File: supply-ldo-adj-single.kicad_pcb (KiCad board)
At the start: 2 copper layers, 31.8 x 33 mm, 15 parts, among them P1 CONN_02X02, P2 CONN_01X03, P3 CONN_02X08, P4 CONN_02X04, P5 CONN_01X01, P6 CONN_01X01, U1 TPS7A4700

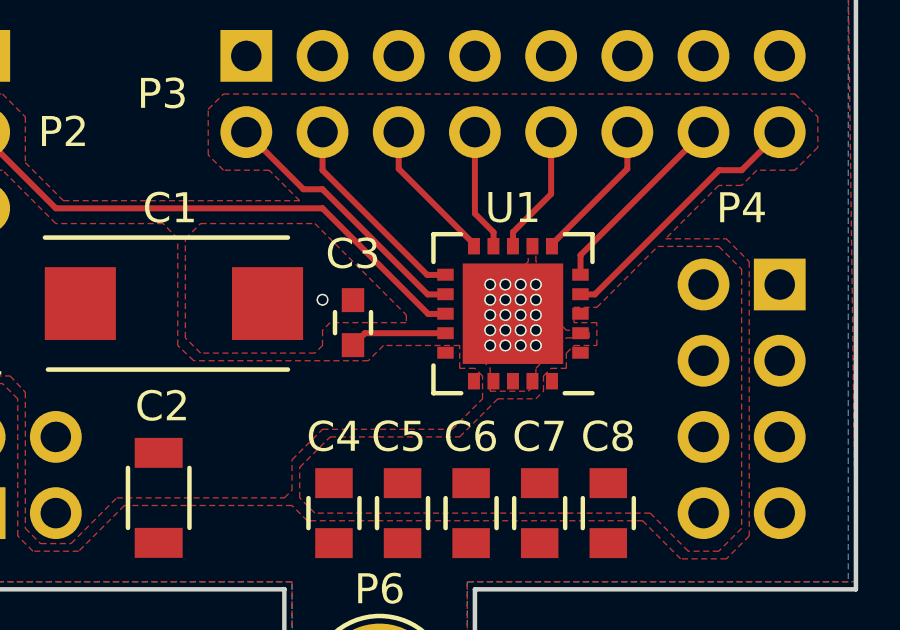
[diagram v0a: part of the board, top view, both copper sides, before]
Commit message: Reduce via size, verbose info on silkscreen
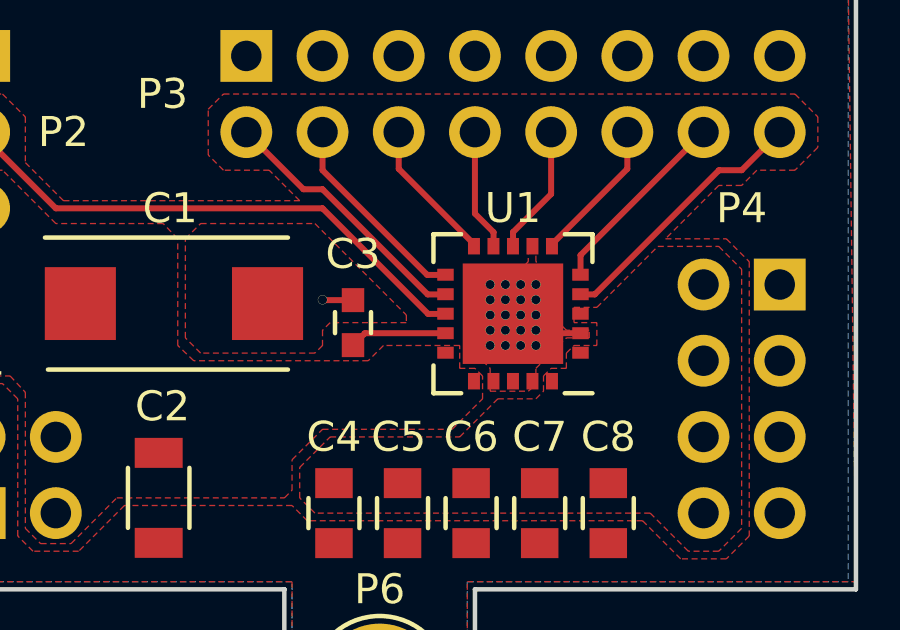
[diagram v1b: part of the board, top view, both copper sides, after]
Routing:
- net GND: track 0.00 -> 2.51 mm
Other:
- net class Thermal added: clearance 0.2, trace_width 0.2, via_dia 0.31, via_drill 0.3
- rule via_min_size: 0.4 -> 0.31
- board text added: "EN"
- board text added: "Low Dropout Adjustable Single Power Supply"
- board text added: "Vadj"
- board text added: "Vin≤36v"
- board text added: "Vout=Vadj+1.6"
- board text removed: "Vin"
- board text removed: "Vout"
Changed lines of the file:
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@@
-(kicad_pcb (version 4) (host pcbnew 4.0.2-stable)
+(kicad_pcb (version 4) (host pcbnew 4.0.1-stable)
   (general
     (links 58)
-    (no_connects 2)
+    (no_connects 0)
     (area 68.551667 20.244999 105.438334 53.934)
     (thickness 1.6)
-    (drawings 22)
-    (tracks 52)
+    (drawings 25)
+    (tracks 56)
     (zones 0)
     (modules 15)
@@
     (via_size 0.4)
     (via_drill 0.3)
-    (via_min_size 0.4)
+    (via_min_size 0.31)
     (via_min_drill 0.3)
     (uvia_size 0.508)
@@
     (pad_to_mask_clearance 0.2)
     (aux_axis_origin 0 0)
-    (visible_elements FFFFFF7F)
+    (visible_elements 7FFFFF5F)
     (pcbplotparams
       (layerselection 0x010fc_80000001)
@@
     (add_net "Net-(P6-Pad1)")
   )
+  (net_class Thermal ""
+    (clearance 0.2)
+    (trace_width 0.2)
+    (via_dia 0.31)
+    (via_drill 0.3)
+    (uvia_dia 0.508)
+    (uvia_drill 0.127)
+  )
   (module Capacitors_Tantalum_SMD:TantalC_SizeD_EIA-7343_Reflow (layer F.Cu)
     (at 80.137 37.465)
@@
       (net 5 "Net-(P6-Pad1)"))
   )
-  (gr_text "GPLv3\n©2016\nNESH@NJIT" (at 86.868 43.688) (layer B.SilkS)
-    (effects (font (size 1 1) (thickness 0.2)) (justify mirror))
-  )
-  (gr_text On (at 76.454 33.02) (layer B.SilkS)
-    (effects (font (size 1 1) (thickness 0.2)) (justify mirror))
-  )
-  (gr_text Off (at 76.708 30.48) (layer B.SilkS)
-    (effects (font (size 1 1) (thickness 0.2)) (justify mirror))
+  (gr_text EN (at 76.2 31.75) (layer B.SilkS)
+    (effects (font (size 0.8 0.8) (thickness 0.2)) (justify mirror))
+  )
+  (gr_text "GPLv3\n©2016\nNESH@NJIT" (at 87.122 44.831) (layer B.SilkS)
+    (effects (font (size 0.8 0.8) (thickness 0.2)) (justify mirror))
+  )
+  (gr_text Vadj (at 91.44 35.433) (layer B.SilkS)
+    (effects (font (size 0.8 0.8) (thickness 0.2)) (justify mirror))
+  )
+  (gr_text "Low Dropout Adjustable\nSingle Power Supply" (at 87.122 40.386) (layer B.SilkS)
+    (effects (font (size 0.8 0.8) (thickness 0.2)) (justify mirror))
+  )
+  (gr_text On (at 76.2 34.29) (layer B.SilkS)
+    (effects (font (size 0.8 0.8) (thickness 0.2)) (justify mirror))
+  )
+  (gr_text Off (at 76.454 29.21) (layer B.SilkS)
+    (effects (font (size 0.8 0.8) (thickness 0.2)) (justify mirror))
   )
   (gr_text ⏚ (at 73.66 46.355) (layer B.SilkS)
@@
     (effects (font (size 1 1) (thickness 0.2)) (justify mirror))
   )
-  (gr_text Vin (at 78.74 43.18) (layer B.SilkS)
-    (effects (font (size 1 1) (thickness 0.2)) (justify mirror))
+  (gr_text Vin≤36v (at 74.93 39.624) (layer B.SilkS)
+    (effects (font (size 0.8 0.8) (thickness 0.2)) (justify mirror))
   )
   (gr_text ⏚ (at 100.33 46.355) (layer B.SilkS)
@@
     (effects (font (size 1 1) (thickness 0.2)) (justify mirror))
   )
-  (gr_text Vout (at 94.488 40.64) (layer B.SilkS)
-    (effects (font (size 1 1) (thickness 0.2)) (justify mirror))
+  (gr_text Vout=Vadj+1.6 (at 95.504 40.64 270) (layer B.SilkS)
+    (effects (font (size 0.8 0.8) (thickness 0.2)) (justify mirror))
   )
   (gr_text "6.4 6.4 3.2 1.6 0.8 0.4 0.2 0.1" (at 91.44 34.036) (layer B.SilkS)
-    (effects (font (size 1 0.85) (thickness 0.2)) (justify mirror))
+    (effects (font (size 0.8 0.8) (thickness 0.2)) (justify mirror))
   )
   (gr_line (start 102.87 46.99) (end 102.87 26.67) (layer Edge.Cuts) (width 0.15))
@@
   (gr_line (start 90.17 26.67) (end 90.17 20.32) (layer Edge.Cuts) (width 0.15))
   (gr_line (start 102.87 26.67) (end 90.17 26.67) (layer Edge.Cuts) (width 0.15))
-  (via (at 85.09 37.338) (size 0.4) (drill 0.3) (layers F.Cu B.Cu) (net 1))
-  (via (at 92.202 38.862) (size 0.4) (drill 0.3) (layers F.Cu B.Cu) (net 1) (status 30))
-  (via (at 91.694 38.862) (size 0.4) (drill 0.3) (layers F.Cu B.Cu) (net 1) (status 30))
-  (via (at 91.186 38.862) (size 0.4) (drill 0.3) (layers F.Cu B.Cu) (net 1) (status 30))
-  (via (at 90.678 38.862) (size 0.4) (drill 0.3) (layers F.Cu B.Cu) (net 1) (status 30))
-  (via (at 92.202 36.83) (size 0.4) (drill 0.3) (layers F.Cu B.Cu) (net 1) (status 30))
-  (via (at 91.694 36.83) (size 0.4) (drill 0.3) (layers F.Cu B.Cu) (net 1) (status 30))
-  (via (at 91.186 36.83) (size 0.4) (drill 0.3) (layers F.Cu B.Cu) (net 1) (status 30))
-  (via (at 90.678 36.83) (size 0.4) (drill 0.3) (layers F.Cu B.Cu) (net 1) (status 30))
-  (via (at 91.694 38.354) (size 0.4) (drill 0.3) (layers F.Cu B.Cu) (net 1) (status 30))
-  (via (at 91.694 37.846) (size 0.4) (drill 0.3) (layers F.Cu B.Cu) (net 1) (status 30))
-  (via (at 91.694 37.338) (size 0.4) (drill 0.3) (layers F.Cu B.Cu) (net 1) (status 30))
-  (via (at 91.186 37.846) (size 0.4) (drill 0.3) (layers F.Cu B.Cu) (net 1) (status 30))
-  (via (at 92.202 37.846) (size 0.4) (drill 0.3) (layers F.Cu B.Cu) (net 1) (status 30))
-  (via (at 92.202 38.354) (size 0.4) (drill 0.3) (layers F.Cu B.Cu) (net 1) (status 30))
-  (via (at 91.186 38.354) (size 0.4) (drill 0.3) (layers F.Cu B.Cu) (net 1) (status 30))
-  (via (at 90.678 38.354) (size 0.4) (drill 0.3) (layers F.Cu B.Cu) (net 1) (status 30))
-  (via (at 90.678 37.846) (size 0.4) (drill 0.3) (layers F.Cu B.Cu) (net 1) (status 30))
-  (via (at 92.202 37.338) (size 0.4) (drill 0.3) (layers F.Cu B.Cu) (net 1) (status 30))
-  (via (at 91.186 37.338) (size 0.4) (drill 0.3) (layers F.Cu B.Cu) (net 1) (status 30))
-  (via (at 90.678 37.338) (size 0.4) (drill 0.3) (layers F.Cu B.Cu) (net 1) (status 30))
+  (segment (start 93.6879 38.4533) (end 92.4629 38.4533) (width 0.2) (layer F.Cu) (net 1))
+  (segment (start 92.4629 38.4533) (end 92.2754 38.6408) (width 0.2) (layer F.Cu) (net 1))
+  (segment (start 86.106 37.35) (end 85.102 37.35) (width 0.2) (layer F.Cu) (net 1))
+  (segment (start 85.102 37.35) (end 85.09 37.338) (width 0.2) (layer F.Cu) (net 1))
+  (via (at 85.09 37.338) (size 0.31) (drill 0.3) (layers F.Cu B.Cu) (net 1))
+  (via (at 92.202 38.862) (size 0.31) (drill 0.3) (layers F.Cu B.Cu) (net 1) (status 30))
+  (via (at 91.694 38.862) (size 0.31) (drill 0.3) (layers F.Cu B.Cu) (net 1) (status 30))
+  (via (at 91.186 38.862) (size 0.31) (drill 0.3) (layers F.Cu B.Cu) (net 1) (status 30))
+  (via (at 90.678 38.862) (size 0.31) (drill 0.3) (layers F.Cu B.Cu) (net 1) (status 30))
+  (via (at 92.202 36.83) (size 0.31) (drill 0.3) (layers F.Cu B.Cu) (net 1) (status 30))
+  (via (at 91.694 36.83) (size 0.31) (drill 0.3) (layers F.Cu B.Cu) (net 1) (status 30))
+  (via (at 91.186 36.83) (size 0.31) (drill 0.3) (layers F.Cu B.Cu) (net 1) (status 30))
+  (via (at 90.678 36.83) (size 0.31) (drill 0.3) (layers F.Cu B.Cu) (net 1) (status 30))
+  (via (at 91.694 38.354) (size 0.31) (drill 0.3) (layers F.Cu B.Cu) (net 1) (status 30))
+  (via (at 91.694 37.846) (size 0.31) (drill 0.3) (layers F.Cu B.Cu) (net 1) (status 30))
+  (via (at 91.694 37.338) (size 0.31) (drill 0.3) (layers F.Cu B.Cu) (net 1) (status 30))
+  (via (at 91.186 37.846) (size 0.31) (drill 0.3) (layers F.Cu B.Cu) (net 1) (status 30))
+  (via (at 92.202 37.846) (size 0.31) (drill 0.3) (layers F.Cu B.Cu) (net 1) (status 30))
+  (via (at 92.202 38.354) (size 0.31) (drill 0.3) (layers F.Cu B.Cu) (net 1) (status 30))
+  (via (at 91.186 38.354) (size 0.31) (drill 0.3) (layers F.Cu B.Cu) (net 1) (status 30))
+  (via (at 90.678 38.354) (size 0.31) (drill 0.3) (layers F.Cu B.Cu) (net 1) (status 30))
+  (via (at 90.678 37.846) (size 0.31) (drill 0.3) (layers F.Cu B.Cu) (net 1) (status 30))
+  (via (at 92.202 37.338) (size 0.31) (drill 0.3) (layers F.Cu B.Cu) (net 1) (status 30))
+  (via (at 91.186 37.338) (size 0.31) (drill 0.3) (layers F.Cu B.Cu) (net 1) (status 30))
+  (via (at 90.678 37.338) (size 0.31) (drill 0.3) (layers F.Cu B.Cu) (net 1) (status 30))
   (segment (start 89.1879 38.4533) (end 86.5027 38.4533) (width 0.2) (layer F.Cu) (net 2))
   (segment (start 86.5027 38.4533) (end 86.106 38.85) (width 0.2) (layer F.Cu) (net 2))

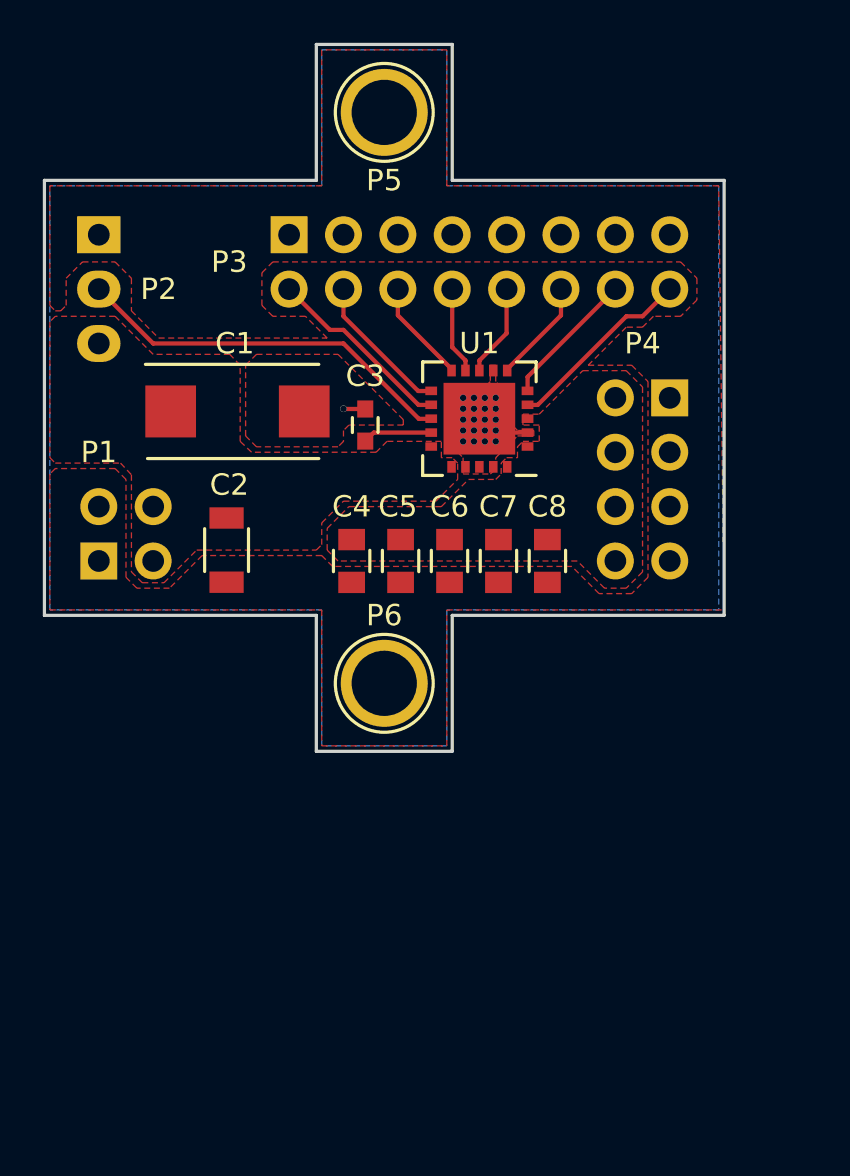
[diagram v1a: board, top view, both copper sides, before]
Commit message: Increase board size, add space for heatsink
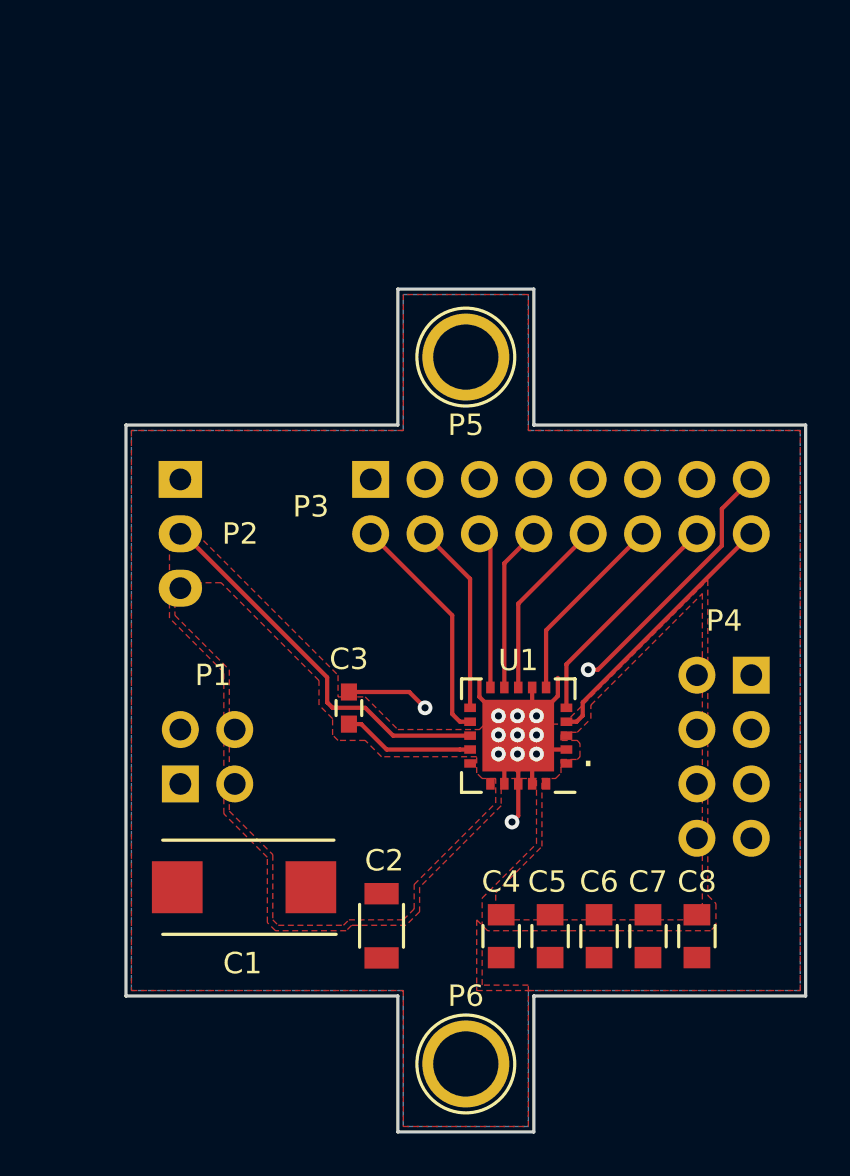
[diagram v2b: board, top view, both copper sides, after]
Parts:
- U1: value TPS7A4700 -> TPS7A4700RGWR
- moved C1 22.2 mm to (80.4, 59.7), turned to 180 degrees
- moved C2 19.0 mm to (86.9, 61.5)
- moved C4 18.9 mm to (92.5, 62.0)
- moved C5 18.9 mm to (94.7, 62.0)
- moved C6 18.9 mm to (97.0, 62.0)
- moved C7 18.9 mm to (99.3, 62.0)
- moved C8 18.9 mm to (101.6, 62.0)
- moved P6 18.2 mm to (90.8, 67.9)
- moved U1 14.9 mm to (93.3, 52.6)
- moved P4 13.5 mm to (104.1, 49.8)
- moved C3 13.2 mm to (85.3, 51.3)
- moved P2 12.0 mm to (77.5, 40.6)
- moved P3 12.0 mm to (86.4, 40.6)
- moved P5 12.0 mm to (90.8, 34.9)
- moved P1 11.1 mm to (77.5, 54.9)
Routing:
- net GND: track 2.51 -> 30.2 mm, vias 21 -> 12
- net Net-(P3-Pad10): track 4.34 -> 8.53 mm
- net Net-(P3-Pad12): track 4.85 -> 9.04 mm
- net Net-(P3-Pad14): track 6.46 -> 10.7 mm
- net Net-(P3-Pad16): track 8.88 -> 12.6 mm
- net Net-(P3-Pad8): track 4.07 -> 7.75 mm
- net Net-(C3-Pad1): track 3.25 -> 6.15 mm
- net Net-(P3-Pad6): track 4.85 -> 7.39 mm
- net Net-(P3-Pad4): track 6.82 -> 9.00 mm
- net Net-(P3-Pad2): track 8.88 -> 11.0 mm
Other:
- board size 31.8 x 33 mm -> 31.8 x 39.4 mm
- net class Default: via_dia 0.4 -> 0.69; via_drill 0.3 -> 0.33
- net class Thermal removed
- rule via_min_drill: 0.3 -> 0.33
- rule via_min_size: 0.31 -> 0.69
- board text added: "."
- board text added: "NESH@NJIT GPLv3©2016"
- board text added: "Single Power Supply Low Dropout Adjustable"
- board text added: "Vout= Vadj+1.6"
- board text removed: "GPLv3 ©2016 NESH@NJIT"
- board text removed: "Low Dropout Adjustable Single Power Supply"
- board text removed: "Vout=Vadj+1.6"

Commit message: Correct Vref to 1.4v
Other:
- board text added: "Vout= Vadj+1.4"
- board text removed: "Vout= Vadj+1.6"
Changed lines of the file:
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@@
-(kicad_pcb (version 4) (host pcbnew 4.0.2-stable)
+(kicad_pcb (version 4) (host pcbnew 4.0.1-stable)
   (general
     (links 58)
     (no_connects 0)
-    (area 74.854999 31.674999 106.755001 71.195001)
+    (area 72.361667 31.674999 109.248334 71.714)
     (thickness 1.6)
     (drawings 26)
@@
     (effects (font (size 1 1) (thickness 0.2)) (justify mirror))
   )
-  (gr_text "Vout=\nVadj+1.6" (at 99.822 53.594) (layer B.SilkS)
+  (gr_text "Vout=\nVadj+1.4" (at 99.822 53.594) (layer B.SilkS)
     (effects (font (size 0.8 0.8) (thickness 0.2)) (justify left mirror))
   )
